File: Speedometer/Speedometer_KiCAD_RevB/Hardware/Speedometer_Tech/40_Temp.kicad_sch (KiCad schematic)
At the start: 18 parts, among them U400 WS2812B-4020_2, U401 WS2812B-4020_2, U402 WS2812B-4020_2, U403 WS2812B-4020_2, U404 WS2812B-4020_2, U405 WS2812B-4020_2, U406 WS2812B-4020_2, U407 WS2812B-4020_2, U410 WS2812B-4020_2, U411 WS2812B-4020_2, U412 WS2812B-4020_2, U413 WS2812B-4020_2, U414 WS2812B-4020_2, U420 WS2812B-4020_2, U421 WS2812B-4020_2, U422 WS2812B-4020_2, U423 WS2812B-4020_2, U424 WS2812B-4020_2

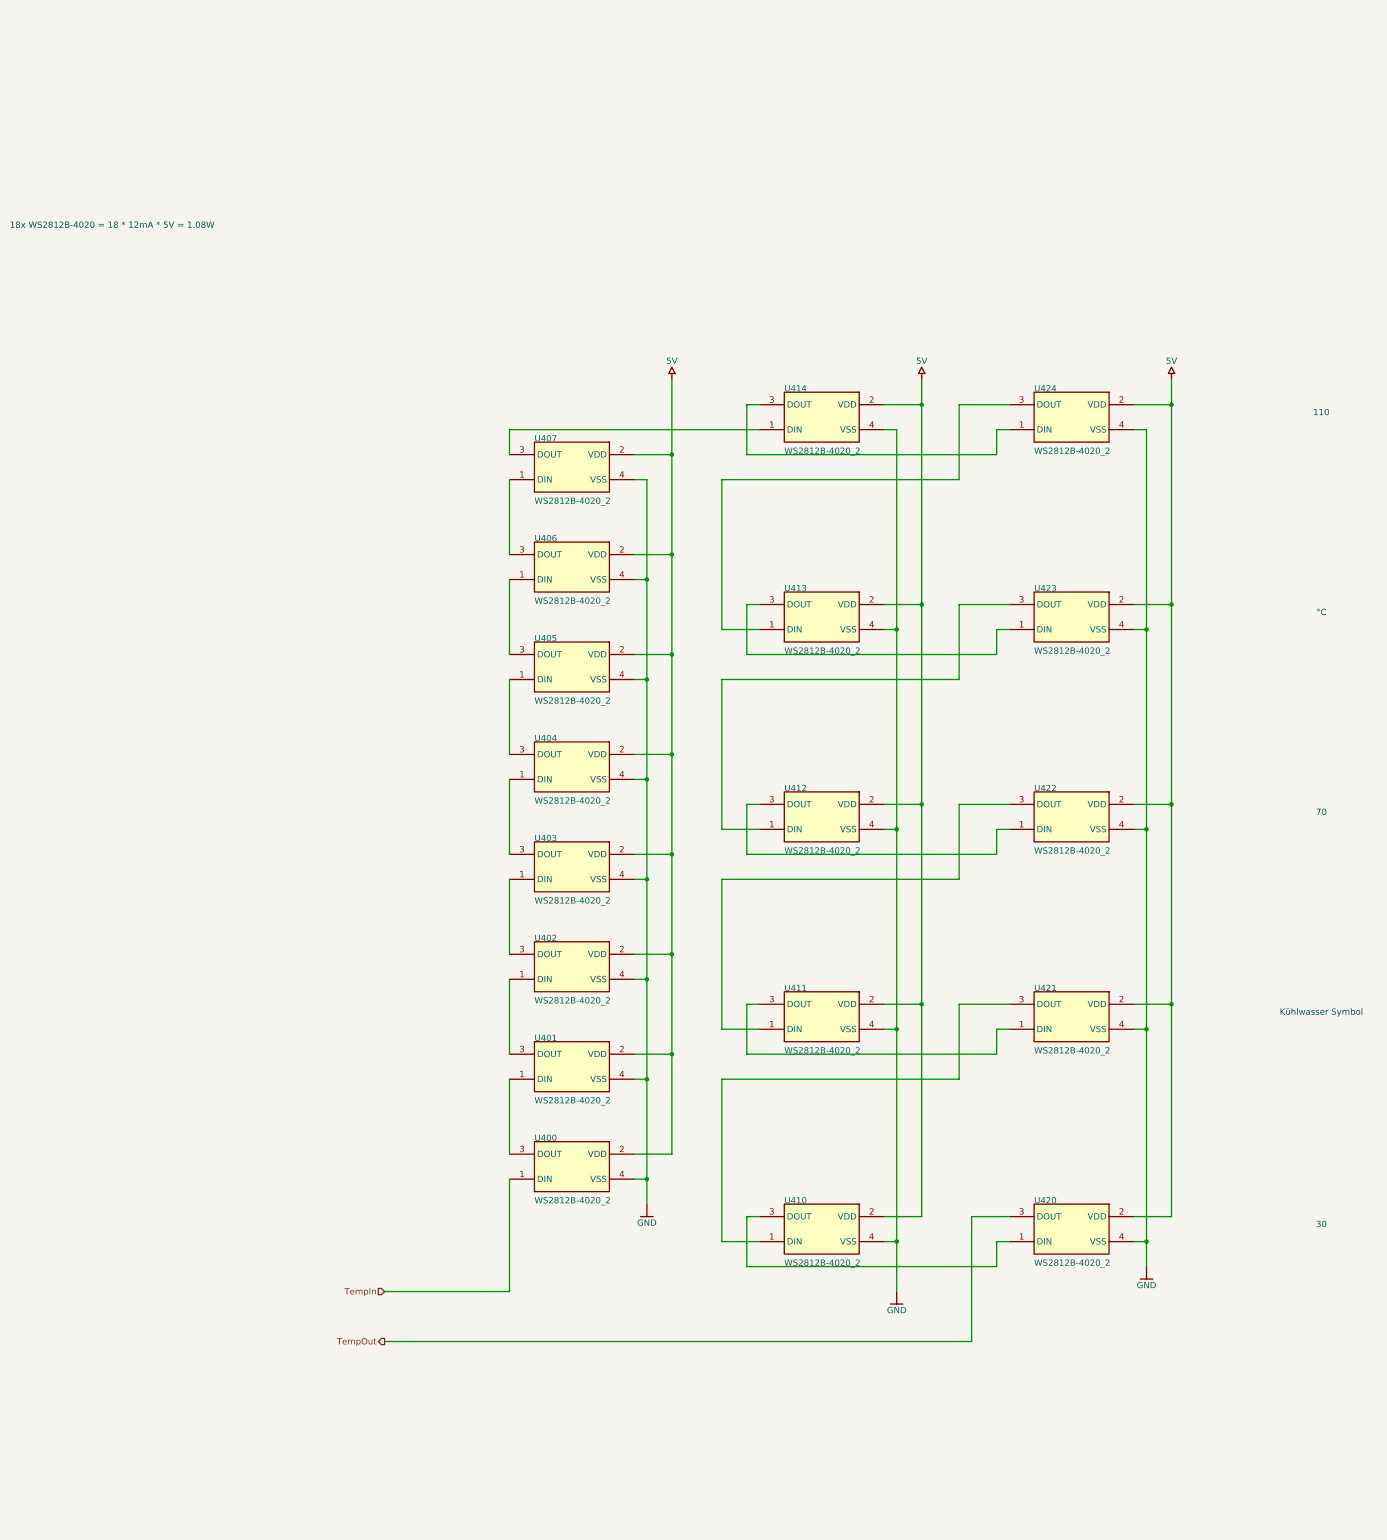
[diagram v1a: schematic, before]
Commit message: current version of lada speedometer in kicad
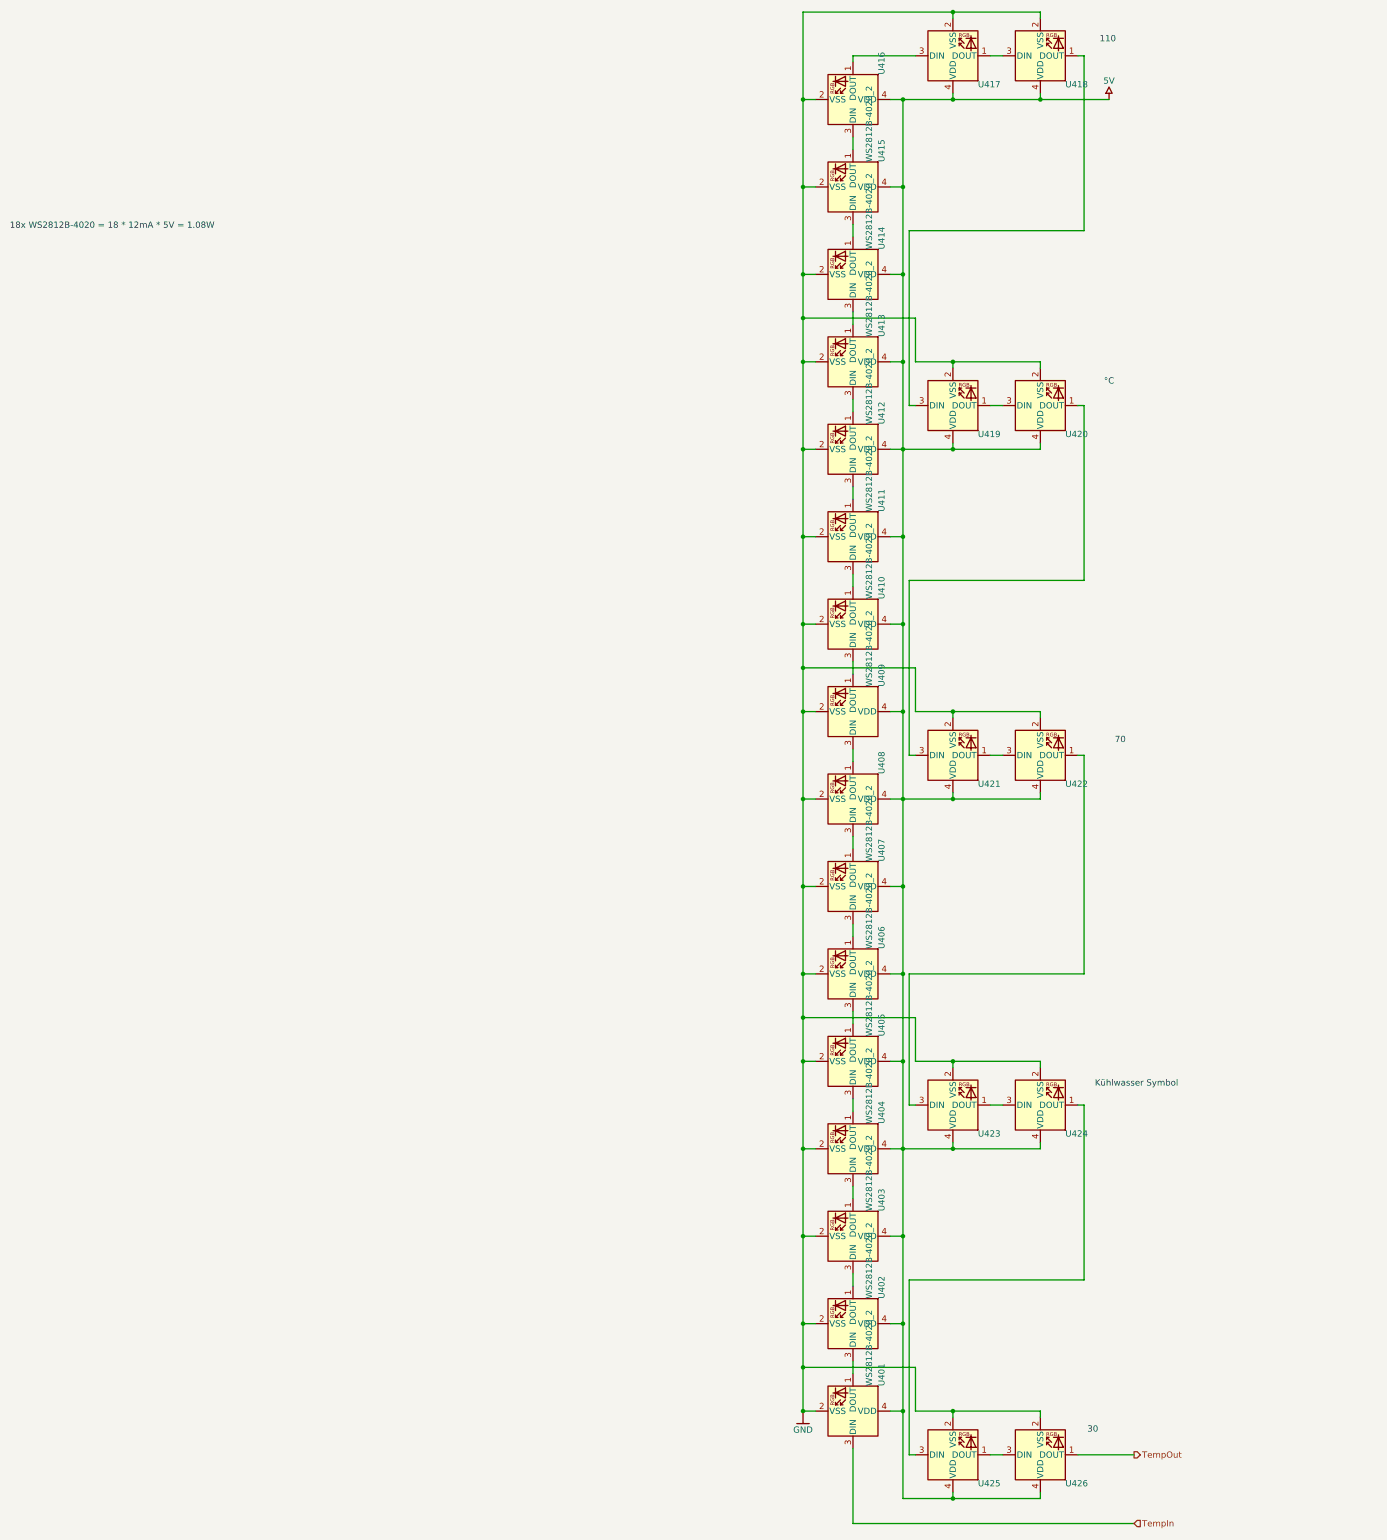
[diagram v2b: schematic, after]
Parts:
- removed U400, U401, U402, U403, U404, U405, U406, U407, U410, U411, U412, U413, U414, U420, U421, U422, U423, U424: WS2812B-4020_2, LED_WS2812B-4020, symbol Speedometer_Tech-altium-import:Designator_0_WS2812B-4020_2
- added U401, U402, U403, U404, U405, U406, U407, U408, U409, U410, U411, U412, U413, U414, U415, U416, U417, U418, U419, U420, U421, U422, U423, U424, U425, U426: WS2812B-4020_2, LED_SMD:LED_WS2812B-2020_PLCC4_2.0x2.0mm, symbol LED:WS2812B-2020
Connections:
- net 5V: now also U401.4 (VDD), U402.4 (VDD), U403.4 (VDD), U404.4 (VDD), U405.4 (VDD), U406.4 (VDD), U407.4 (VDD), U408.4 (VDD), U409.4 (VDD), U410.4 (VDD), U411.4 (VDD), U412.4 (VDD), U413.4 (VDD), U414.4 (VDD), U415.4 (VDD), U416.4 (VDD), U417.4 (VDD), U418.4 (VDD), U419.4 (VDD), U420.4 (VDD), U421.4 (VDD), U422.4 (VDD), U423.4 (VDD), U424.4 (VDD), U425.4 (VDD), U426.4 (VDD)
- net GND: now also U401.2 (VSS), U402.2 (VSS), U403.2 (VSS), U404.2 (VSS), U405.2 (VSS), U406.2 (VSS), U407.2 (VSS), U408.2 (VSS), U409.2 (VSS), U410.2 (VSS), U411.2 (VSS), U412.2 (VSS), U413.2 (VSS), U414.2 (VSS), U415.2 (VSS), U416.2 (VSS), U417.2 (VSS), U418.2 (VSS), U419.2 (VSS), U420.2 (VSS), U421.2 (VSS), U422.2 (VSS), U423.2 (VSS), U424.2 (VSS), U425.2 (VSS), U426.2 (VSS)
- net TempIn: now also U401.3 (DIN)
- net TempOut: now also U426.1 (DOUT)
- new net: U425.1 (DOUT), U426.3 (DIN)
- new net: U424.1 (DOUT), U425.3 (DIN)
- new net: U421.1 (DOUT), U422.3 (DIN)
- new net: U420.1 (DOUT), U421.3 (DIN)
- new net: U401.1 (DOUT), U402.3 (DIN)
- new net: U418.1 (DOUT), U419.3 (DIN)
- new net: U417.1 (DOUT), U418.3 (DIN)
- new net: U403.1 (DOUT), U404.3 (DIN)
- new net: U402.1 (DOUT), U403.3 (DIN)
- new net: U422.1 (DOUT), U423.3 (DIN)
- new net: U416.1 (DOUT), U417.3 (DIN)
- new net: U415.1 (DOUT), U416.3 (DIN)
- new net: U413.1 (DOUT), U414.3 (DIN)
- new net: U412.1 (DOUT), U413.3 (DIN)
- new net: U411.1 (DOUT), U412.3 (DIN)
- new net: U410.1 (DOUT), U411.3 (DIN)
- new net: U405.1 (DOUT), U406.3 (DIN)
- new net: U404.1 (DOUT), U405.3 (DIN)
- new net: U408.1 (DOUT), U409.3 (DIN)
- new net: U407.1 (DOUT), U408.3 (DIN)
- new net: U419.1 (DOUT), U420.3 (DIN)
- new net: U406.1 (DOUT), U407.3 (DIN)
- new net: U414.1 (DOUT), U415.3 (DIN)
- new net: U423.1 (DOUT), U424.3 (DIN)
- new net: U409.1 (DOUT), U410.3 (DIN)
